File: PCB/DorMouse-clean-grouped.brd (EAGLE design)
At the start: 63.3 x 90.1 mm, 55 parts, among them IC1 LM340MP-05, IC2 MAX1551, U1 STM32F10XRXT6, X1 MINI-USB-UX60-MB-5ST

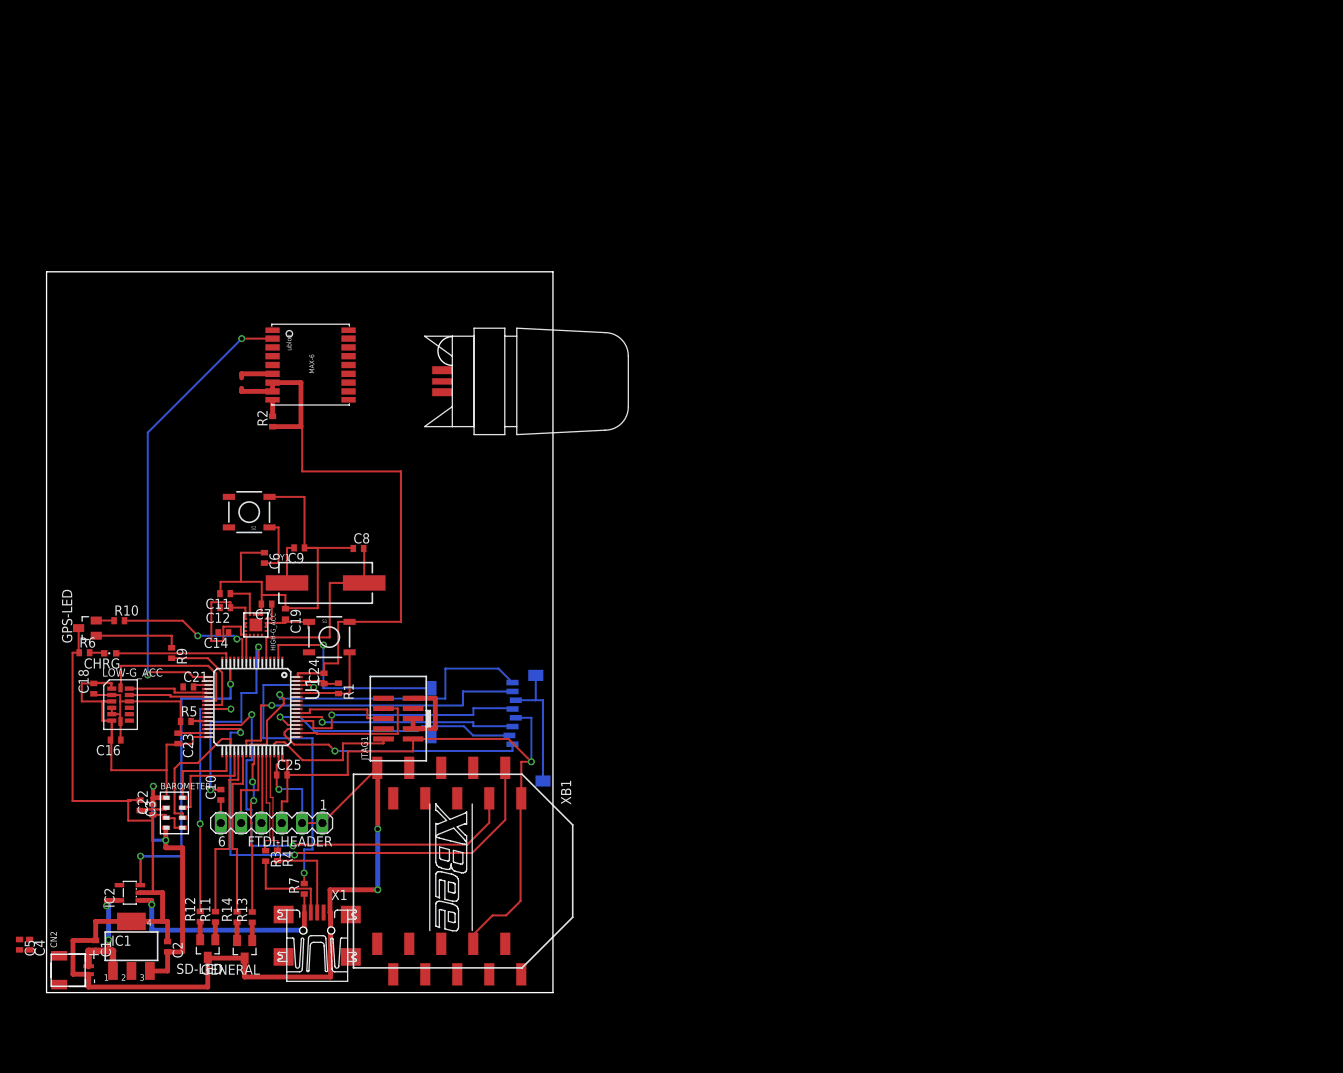
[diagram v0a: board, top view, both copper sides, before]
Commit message: Multiple fixes to schematic, addition of pdf, clean board and partslist.
Ava library fixed: open and save, then it works (?)

Ran ERC: complained about missing joins and signals near each other without
being connected. Discovered one case where something that should be
conected was not. Fixed, then as a precautionary measure, added join
dots everywhere (sorry).

Wrong antenna footprint. Swapped.

Adam says the two-capacitors-with-different-values thing is to do with
response to different frequencies. Added datasheet recommended capacitor
values for the STM analogue.

Adjusted capacitor count for low g accel.

Add parts list
Add schematic PDF
Add 'clean, with groups of easy things routed' board.

Warning: I (foolishly) did the schematic modifications with the clean
board open. This de-synced the board, so I manually re synced them
afterwards, and eagle is now content. Hopefully crazy rubbish won't
happen.
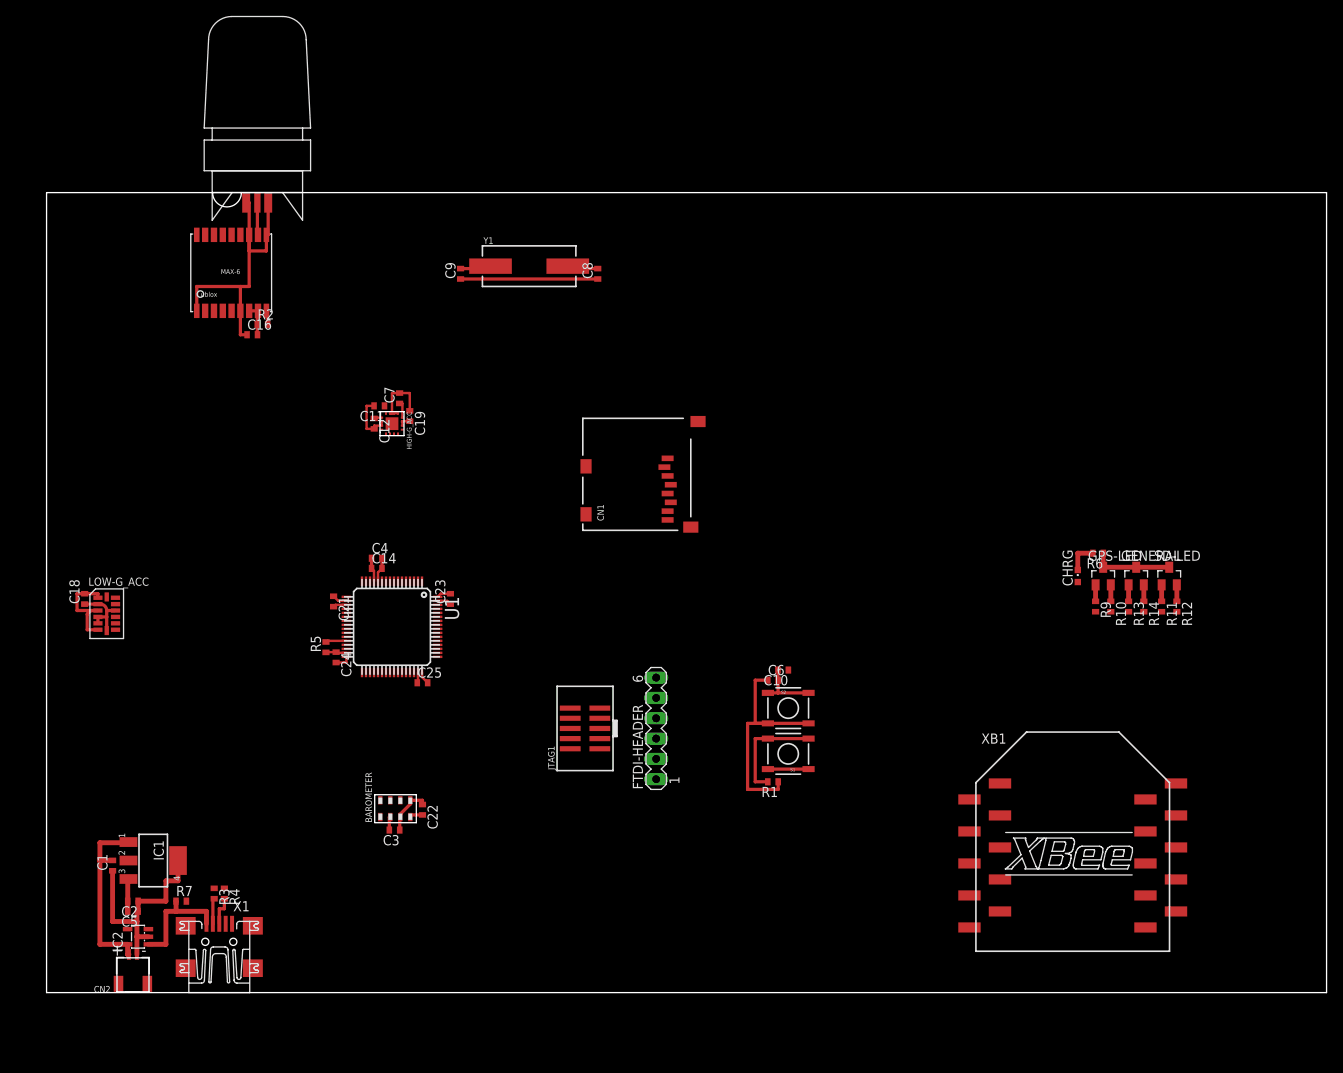
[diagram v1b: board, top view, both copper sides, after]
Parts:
- GPS: device Swallow:UBLOX_MAX-6 -> Ava:UBLOX_MAX-6
- moved SD-LED 128.9 mm to (140.3, 52.1), turned to 0 degrees
- moved R12 128.1 mm to (141.3, 48.3), turned to 270 degrees
- moved R6 127.3 mm to (131.4, 54.9), turned to 180 degrees
- moved GPS-LED 127.1 mm to (132.1, 52.1), turned to 0 degrees
- moved R11 124.5 mm to (139.4, 48.3), turned to 270 degrees
- moved R10 124.0 mm to (133.0, 48.3), turned to 270 degrees
- moved CHRG 121.3 mm to (128.9, 52.1), turned to 0 degrees
- moved GENERAL 120.8 mm to (136.2, 52.1), turned to 0 degrees
- moved R14 119.8 mm to (137.2, 48.3), turned to 270 degrees
- moved R13 116.2 mm to (135.3, 48.3), turned to 270 degrees
- moved R9 115.6 mm to (131.1, 48.3)
- moved XB1 78.0 mm to (128.3, 17.1), turned to 0 degrees
- moved C10 72.0 mm to (92.1, 40.3), turned to 180 degrees
- moved S2 71.7 mm to (92.7, 35.6), turned to 0 degrees
- moved C6 65.4 mm to (90.8, 39.1), turned to 0 degrees
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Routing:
- net VCC: track 247.8 -> 39.4 mm, vias 3 -> 0
- net GND: track 294.8 -> 162.2 mm, vias 3 -> 0
- net U3-RX: track 63.9 -> 0.00 mm, vias 2 -> 0
- net U2-RX: track 58.7 -> 0.00 mm, vias 2 -> 0
- net U3-TX: track 57.8 -> 0.00 mm, vias 2 -> 0
- net SD-DAT1: track 44.5 -> 0.00 mm, vias 1 -> 0
- net SD-DAT0: track 40.9 -> 0.00 mm, vias 1 -> 0
- net N$21: track 40.9 -> 0.00 mm, vias 2 -> 0
- net CHARGING(-): track 39.3 -> 0.00 mm, vias 2 -> 0
- net SD-DAT3: track 32.7 -> 0.00 mm, vias 1 -> 0
- net SD-DAT2: track 32.4 -> 0.00 mm, vias 1 -> 0
- net SD_:): track 32.2 -> 0.00 mm, vias 2 -> 0
- net SD-CLK: track 30.3 -> 0.00 mm, vias 1 -> 0
- net SD-CMD: track 28.0 -> 0.00 mm, vias 1 -> 0
- net RESET: track 34.7 -> 7.98 mm, vias 2 -> 0
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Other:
- board size 63.3 x 90.1 mm -> 160 x 100 mm

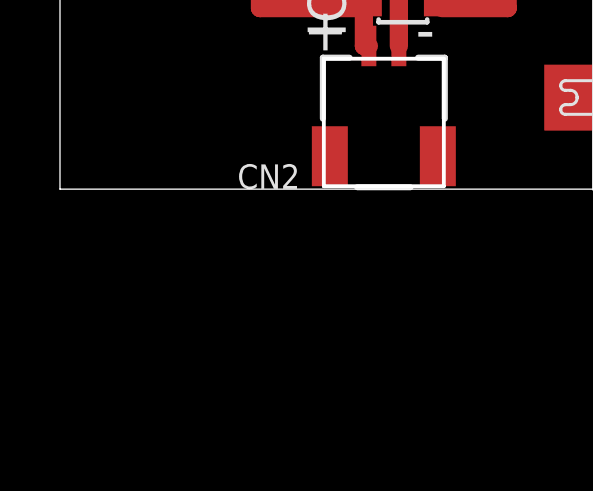
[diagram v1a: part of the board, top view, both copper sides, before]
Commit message: Add resistor and cap, reverse ADC connections. Warning: desync
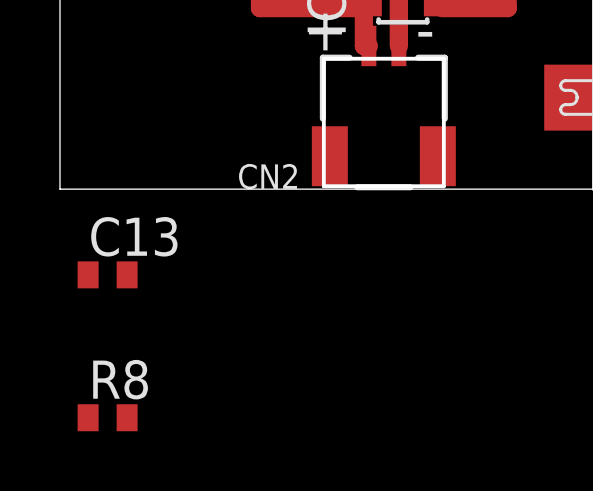
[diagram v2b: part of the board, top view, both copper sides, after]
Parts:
- added C13: 1uF, rcl:C0402
- added R8: 100k, rcl:R0402
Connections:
- new net N$13: IC2.3, R8.1
- net CHARGING(-): now also R8.2; no longer IC2.3
- net GND: now also C13.1
- net USB-5V: now also C13.2
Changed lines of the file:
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@@
 <element name="C4" library="rcl" package="C0402" value="10nF" x="41.275" y="54.2925"/>
 <element name="C5" library="rcl" package="C0402" value="4.7uF" x="10.795" y="10.16" rot="R180"/>
+<element name="C13" library="rcl" package="C0402" value="1uF" x="1.5875" y="-2.8575"/>
+<element name="R8" library="rcl" package="R0402" value="100k" x="1.5875" y="-7.62"/>
 </elements>
 <signals>
@@
 <wire x1="87.63" y1="25.4" x2="91.455" y2="25.4" width="0.4064" layer="1"/>
 <wire x1="91.455" y1="25.4" x2="91.455" y2="26.3525" width="0.4064" layer="1"/>
+<contactref element="C13" pad="1"/>
 <wire x1="95.25" y1="33.655" x2="132.08" y2="53.17" width="0" layer="19" extent="1-1"/>
 <wire x1="76.2" y1="26.67" x2="87.63" y2="25.4" width="0" layer="19" extent="1-1"/>
@@
 <wire x1="23.19" y1="8.6" x2="44.1475" y2="20.32" width="0" layer="19" extent="1-1"/>
 <wire x1="16.434" y1="13.97" x2="23.19" y2="8.6" width="0" layer="19" extent="1-1"/>
+<wire x1="0.9375" y1="-2.8575" x2="11.295" y2="4.7725" width="0" layer="19" extent="1-1"/>
 <wire x1="8.62" y1="47.76" x2="34.925" y2="42.53" width="0" layer="19" extent="1-1"/>
 <wire x1="115.362" y1="8.145" x2="91.455" y2="25.4" width="0" layer="19" extent="1-1"/>
@@
 <wire x1="16.1775" y1="11.43" x2="16.1925" y2="11.43" width="0.6096" layer="1"/>
 <wire x1="16.1925" y1="11.43" x2="16.1925" y2="10.16" width="0.6096" layer="1"/>
+<contactref element="C13" pad="2"/>
+<wire x1="2.2375" y1="-2.8575" x2="12.73" y2="6.035" width="0" layer="19" extent="1-1"/>
 </signal>
 <signal name="CHARGING(-)">
-<contactref element="IC2" pad="3"/>
 <contactref element="U1" pad="14"/>
-<wire x1="12.73" y1="7.935" x2="40.43" y2="51.42" width="0" layer="19" extent="1-1"/>
+<contactref element="R8" pad="2"/>
+<wire x1="2.2375" y1="-7.62" x2="40.43" y2="51.42" width="0" layer="19" extent="1-1"/>
 </signal>
 <signal name="MOSI-1">
@@
 <wire x1="17.4775" y1="11.43" x2="48.88" y2="48.47" width="0" layer="19" extent="1-1"/>
 </signal>
+<signal name="N$13">
+<contactref element="IC2" pad="3"/>
+<contactref element="R8" pad="1"/>
+<wire x1="0.9375" y1="-7.62" x2="12.73" y2="7.935" width="0" layer="19" extent="1-1"/>
+</signal>
 </signals>
